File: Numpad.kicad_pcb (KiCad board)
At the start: 2 copper layers, 82.6 x 127 mm, 68 parts, among them J1 SWD, J2 USB_C_Receptacle_USB2.0, U1 SRV05-4, U2 STM32F103C8Tx, U3 XC6206PxxxMR, Y1 8MHz

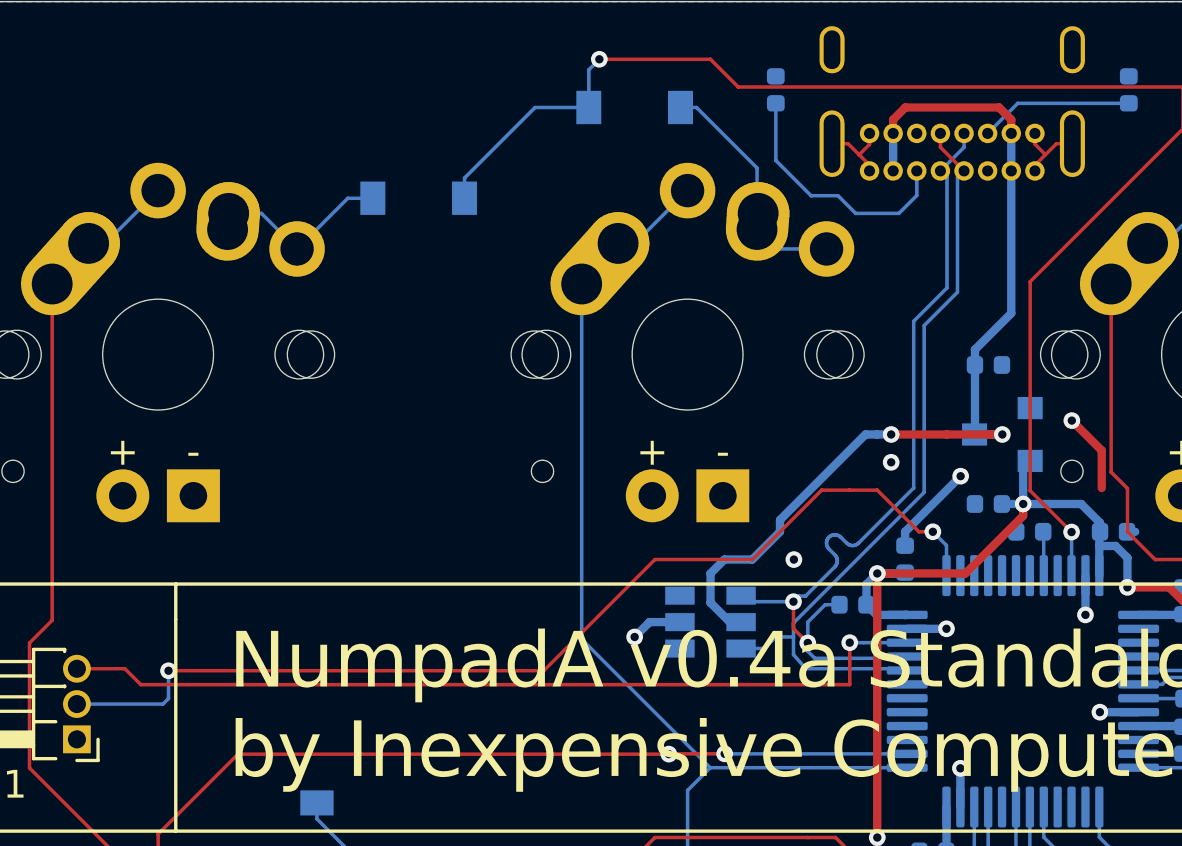
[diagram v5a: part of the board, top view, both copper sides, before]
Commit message: Updated position of ESD protection diodes
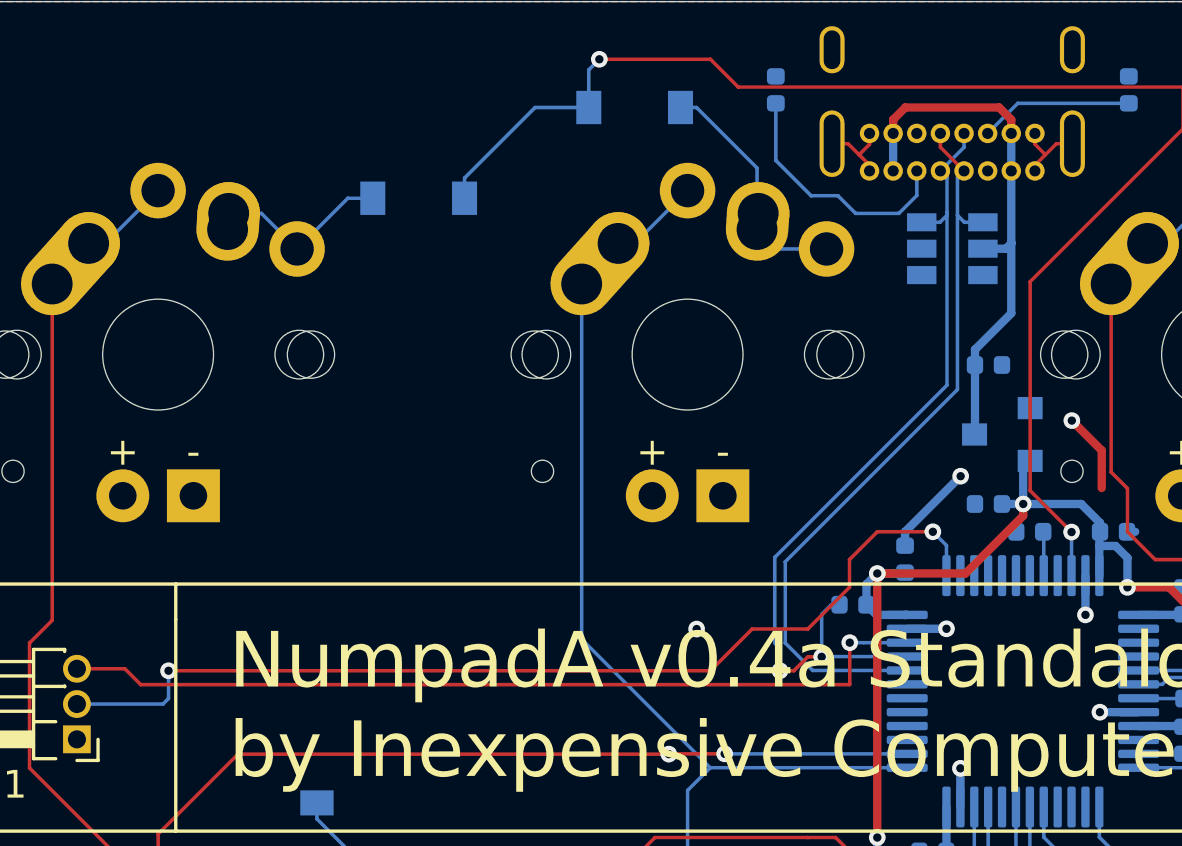
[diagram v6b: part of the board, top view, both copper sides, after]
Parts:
- moved U1 16.0 mm to (139.7, 43.8)
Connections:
- U1 pad 3: (no net) -> DA+
- U1 pad 4: DA+ -> DA-
- U1 pad 6: DA- -> (no net)
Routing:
- net +5V: track 34.6 -> 19.5 mm, vias 2 -> 0
- net GND: track 25.2 -> 23.3 mm, vias 13 -> 11
- net DA-: track 28.1 -> 27.3 mm
- net SWDCLK: track 37.0 -> 36.3 mm

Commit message: fixed some routing
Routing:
- net GND: track 23.3 -> 24.5 mm
- net /CC1: track 9.07 -> 8.35 mm
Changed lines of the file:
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@@
     (thickness 1.6)
     (drawings 16)
-    (tracks 527)
+    (tracks 528)
     (zones 0)
     (modules 68)
@@
     (tags SOT-23-6)
     (attr smd)
-    (fp_text reference U1 (at 0 2.9) (layer B.SilkS)
+    (fp_text reference U1 (at 2.8 0.185 90) (layer B.SilkS)
       (effects (font (size 1 1) (thickness 0.15)) (justify mirror))
     )
@@
     (descr "USB 2.0 Type C Receptacle, https://gct.co/Files/Drawings/USB4085.pdf")
     (tags "USB Type-C Receptacle Through-hole Right angle")
-    (fp_text reference J2 (at 2.975 1.8) (layer B.SilkS)
+    (fp_text reference J2 (at 9.27836 -1.01718 90) (layer B.SilkS)
       (effects (font (size 1 1) (thickness 0.15)) (justify mirror))
     )
@@
   (segment (start 145.985 54) (end 146.28 54) (width 0.3) (layer B.Cu) (net 11))
   (via (at 130.5 57.5) (size 0.6) (drill 0.3) (layers F.Cu B.Cu) (net 11))
+  (segment (start 138.6 43.815) (end 137.685 43.815) (width 0.3) (layer B.Cu) (net 11))
+  (segment (start 137.685 43.815) (end 137.5 44) (width 0.3) (layer B.Cu) (net 11))
   (segment (start 140.515 50.485) (end 140.5 50.5) (width 0.3) (layer B.Cu) (net 12))
   (segment (start 140.515 48) (end 140.515 50.485) (width 0.3) (layer B.Cu) (net 12))
@@
   (segment (start 141.82164 43.59836) (end 141.82164 46.13836) (width 0.3) (layer B.Cu) (net 12))
   (segment (start 141.82164 41.01718) (end 141.82164 43.59836) (width 0.3) (layer B.Cu) (net 12))
-  (segment (start 138.42164 41.01718) (end 138.42164 41.90164) (width 0.127) (layer B.Cu) (net 13) (status 10))
-  (segment (start 138.42164 41.90164) (end 137.77828 42.545) (width 0.127) (layer B.Cu) (net 13))
-  (segment (start 136.223643 42.545) (end 135.588643 41.91) (width 0.127) (layer B.Cu) (net 13))
-  (segment (start 137.77828 42.545) (end 136.223643 42.545) (width 0.127) (layer B.Cu) (net 13))
-  (segment (start 135.588643 41.91) (end 134.62 41.91) (width 0.127) (layer B.Cu) (net 13))
-  (segment (start 133.35 40.64) (end 133.35 38.585) (width 0.127) (layer B.Cu) (net 13) (status 20))
   (segment (start 134.62 41.91) (end 133.35 40.64) (width 0.127) (layer B.Cu) (net 13))
-  (segment (start 142.05382 38.585) (end 140.97164 39.66718) (width 0.127) (layer B.Cu) (net 14) (status 20))
-  (segment (start 146.05 38.585) (end 142.05382 38.585) (width 0.127) (layer B.Cu) (net 14) (status 10))
+  (segment (start 138.09 41.91) (end 134.62 41.91) (width 0.127) (layer B.Cu) (net 13))
+  (segment (start 138.42164 41.01718) (end 138.42164 41.57836) (width 0.127) (layer B.Cu) (net 13))
+  (segment (start 133.35 40.64) (end 133.35 38.585) (width 0.127) (layer B.Cu) (net 13))
+  (segment (start 138.42164 41.57836) (end 138.09 41.91) (width 0.127) (layer B.Cu) (net 13))
+  (segment (start 140.97164 39.02836) (end 140.97164 39.66718) (width 0.127) (layer B.Cu) (net 14))
+  (segment (start 146.05 38.585) (end 141.415 38.585) (width 0.127) (layer B.Cu) (net 14))
+  (segment (start 141.415 38.585) (end 140.97164 39.02836) (width 0.127) (layer B.Cu) (net 14))
   (segment (start 139.485 63.9075) (end 139.49 63.9025) (width 0.127) (layer B.Cu) (net 15))
   (segment (start 138.0575 56.97) (end 138.0775 56.99) (width 0.127) (layer B.Cu) (net 15))

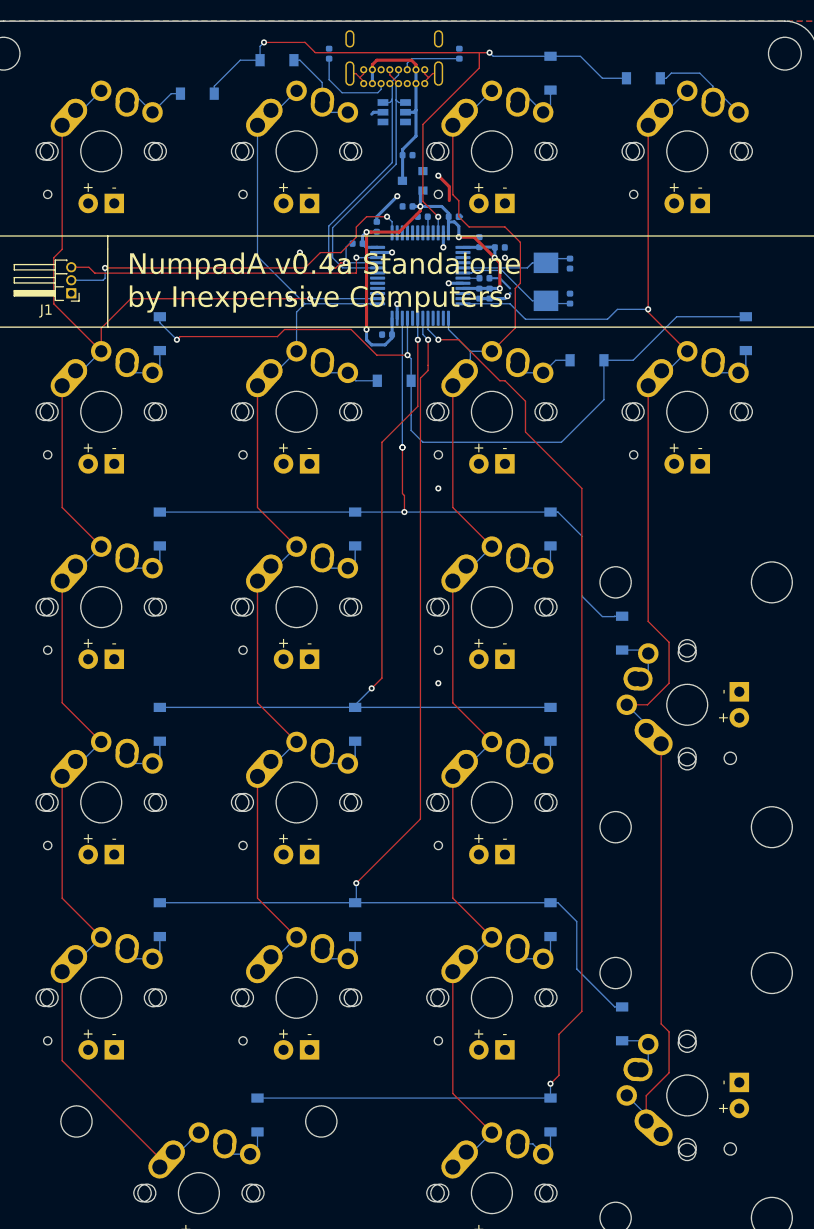
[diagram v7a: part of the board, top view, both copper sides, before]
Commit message: Changed LEDs to SOD323
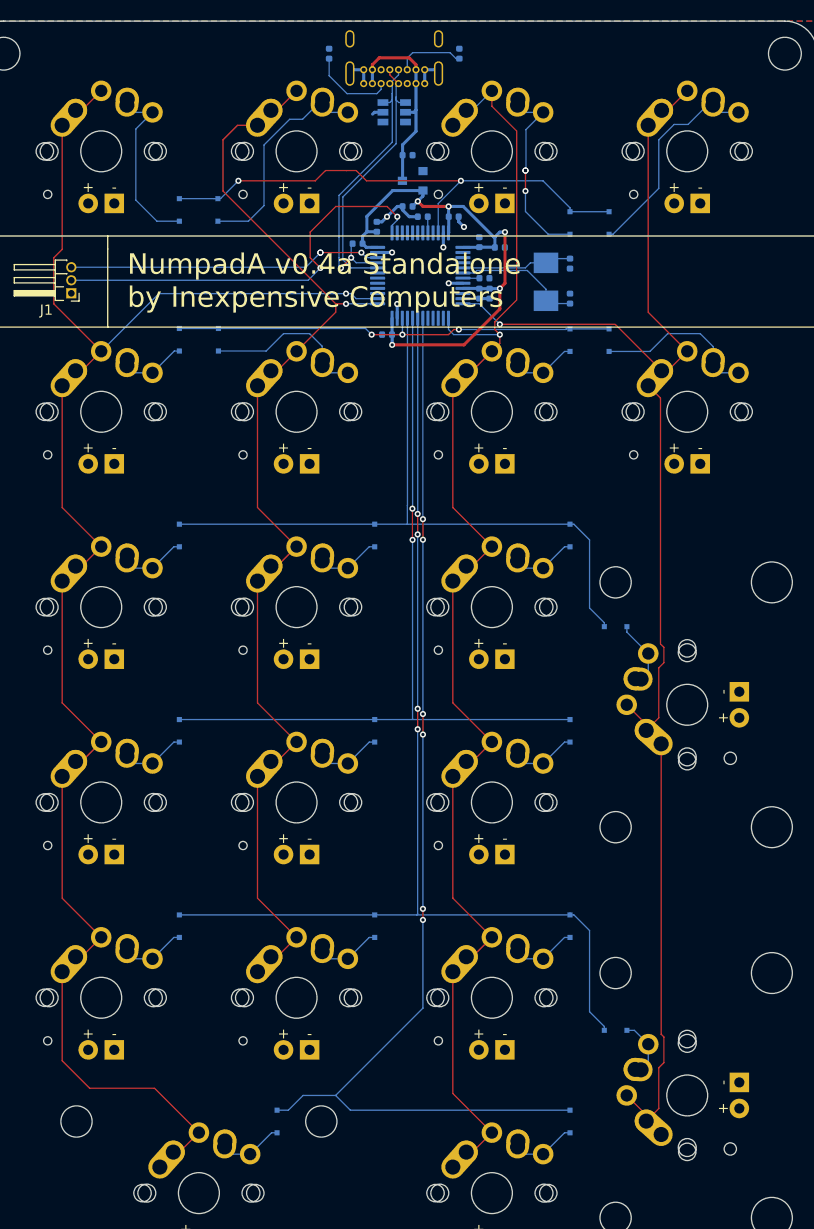
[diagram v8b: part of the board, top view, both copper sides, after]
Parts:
- D_0, D_1, D_2, D_3, D_4, D_5, D_6, D_7, D_8, D_9, D_BKSP1, D_DOT1, D_ENTER1, D_ESC1, D_FN1, D_MINUS1, D_NUMLK1, D_PLUS1, D_SLASH1, D_STAR1, D_TAB1: footprint Diode_SMD:D_SOD-123 -> Diode_SMD:D_SOD-323F
- moved D_SLASH1 17.6 mm to (122.6, 66.0), turned to 270 degrees
- moved D_TAB1 15.7 mm to (122.5, 53.3), turned to 270 degrees
- moved D_FN1 14.7 mm to (156.8, 54.6)
- moved D_BKSP1 14.5 mm to (160.7, 54.6), turned to 270 degrees
- moved D_MINUS1 13.4 mm to (160.7, 66.0)
- moved D_ESC1 11.5 mm to (118.7, 53.3), turned to 270 degrees
- moved D_STAR1 2.57 mm to (156.8, 66.0), turned to 270 degrees
- moved D_0 2.01 mm to (128.3, 142.2)
- moved D_DOT1 2.01 mm to (156.8, 142.2)
- moved D_4 2.01 mm to (118.7, 104.1)
- moved D_5 2.01 mm to (137.8, 104.1)
- moved D_6 2.01 mm to (156.8, 104.1)
- moved D_7 2.01 mm to (118.7, 85.1)
- moved D_8 2.01 mm to (137.8, 85.1)
- moved D_9 2.01 mm to (156.8, 85.1)
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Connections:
- U2 pad 17: row6 -> (no net)
- U2 pad 18: row5 -> row6
- U2 pad 19: row4 -> row5
- U2 pad 20: (no net) -> row4
- U2 pad 21: row2 -> row3
- U2 pad 22: row3 -> row2
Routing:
- net row2: track 78.4 -> 44.0 mm, vias 2 -> 3
- net row1: track 65.8 -> 50.9 mm, vias 3 -> 2
- net Net-(D_FN1-Pad2): track 5.46 -> 18.4 mm, vias 0 -> 3
- net Net-(D_TAB1-Pad2): track 8.66 -> 21.1 mm
- net Net-(D_MINUS1-Pad2): track 5.26 -> 16.1 mm
- net Net-(D_ESC1-Pad2): track 6.47 -> 17.1 mm
- net Net-(D_SLASH1-Pad2): track 5.99 -> 16.0 mm
- net Net-(D_BKSP1-Pad2): track 11.9 -> 20.9 mm
- net VBAT: track 51.0 -> 56.7 mm, vias 6 -> 5
- net GND: track 24.5 -> 19.9 mm, vias 11 -> 6
- net row6: track 113.6 -> 109.1 mm, vias 2 -> 6
- net SWDCLK: track 36.3 -> 40.4 mm
- net col2: track 99.6 -> 103.0 mm, vias 0 -> 1
- net row5: track 112.2 -> 109.4 mm, vias 2 -> 4
- net col4: track 128.7 -> 131.4 mm
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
